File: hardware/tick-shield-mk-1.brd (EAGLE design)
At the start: 62 x 52 mm, 15 parts, among them IC1 DS1307, Y1 32.768kHz

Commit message: shieldify all the things
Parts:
- removed C3: 1uF, A_butts:C0805
- removed DISPLAY3, DISPLAY4: 7SEG_4DIGIT_COLON_APOS, A_butts:7SEG_4DIG_10MM
- removed Y1: 32.768kHz, A_butts:TC26H
- added R1, R2: 4.7k, A_butts:R0603
- C2: value 0.1uF -> 1uF; device A_butts:C0603 -> A_butts:C0805
- DISPLAY2: value 7SEG_4DIGIT_COLON_APOS -> 7SEG_4DIGIT_COLON14.2MM-CC; device A_butts:7SEG_4DIG_10MM -> A_butts:7SEG_4DIG_0.56IN_14MM_ADAFRUIT
- IC1: value DS1307 -> DS1338C; device A_butts:DIL08 -> A_butts:SO16W
- moved IC1 26.9 mm to (6.50, 35.5), flipped to the bottom, turned to 0 degrees
- moved C1 26.4 mm to (7.50, 28.0), flipped to the bottom
- moved BAT1 24.4 mm to (8.00, 16.5)
- moved C2 24.0 mm to (32.0, 47.0)
- moved H4 20.0 mm to (48.5, 49.5)
- moved SHIELD 20.0 mm to (6.00, 1.87)
- moved H3 20.0 mm to (48.5, 2.50)
- moved DISPLAY1 15.0 mm to (25.5, 35.5)
- moved H2 9.06 mm to (2.50, 49.5)
- moved H1 9.00 mm to (2.50, 2.50)
- moved DISPLAY2 8.51 mm to (25.5, 16.5)
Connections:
- removed net D10: DISPLAY1.P$13, DISPLAY2.14, DISPLAY3.1, SHIELD.D10
- removed net D11: DISPLAY1.P$9, DISPLAY2.16, DISPLAY3.2, SHIELD.D11
- removed net D12: DISPLAY1.P$4, DISPLAY2.13, DISPLAY3.6, SHIELD.D12
- removed net D13: DISPLAY1.P$2, DISPLAY2.3, DISPLAY3.8, SHIELD.D13
- removed net N$1: IC1.2, Y1.2
- removed net N$2: IC1.1, Y1.1
- net A0: now also DISPLAY1.P$13, DISPLAY2.P$1; no longer DISPLAY1.P$1, DISPLAY2.5, DISPLAY4.1
- net A1: now also DISPLAY1.P$9, DISPLAY2.P$12; no longer DISPLAY1.P$12, DISPLAY2.11, DISPLAY4.2
- net A2: now also DISPLAY1.P$4, DISPLAY2.P$5; no longer DISPLAY1.P$5, DISPLAY2.15, DISPLAY4.6
- net A3: now also DISPLAY1.P$2, DISPLAY2.P$3; no longer DISPLAY1.P$3, DISPLAY2.7, DISPLAY4.8
- net D2: now also DISPLAY1.P$1, DISPLAY2.P$14; no longer DISPLAY1.P$14, DISPLAY3.14, DISPLAY4.14
- net D3: now also DISPLAY1.P$12, DISPLAY2.P$11; no longer DISPLAY1.P$11, DISPLAY3.16, DISPLAY4.16
- net D4: now also DISPLAY1.P$5, DISPLAY2.P$10; no longer DISPLAY1.P$10, DISPLAY3.13, DISPLAY4.13
- net D5: now also DISPLAY1.P$3, DISPLAY2.P$6; no longer DISPLAY1.P$6, DISPLAY3.3, DISPLAY4.3
- net D6: now also DISPLAY1.P$14, DISPLAY2.P$13; no longer DISPLAY2.1, DISPLAY3.5, DISPLAY4.5
- net D7: now also DISPLAY1.P$11, DISPLAY2.P$9; no longer DISPLAY2.2, DISPLAY3.11, DISPLAY4.11
- net D8: now also DISPLAY1.P$10, DISPLAY2.P$4; no longer DISPLAY2.6, DISPLAY3.15, DISPLAY4.15
- net D9: now also DISPLAY1.P$6, DISPLAY2.P$2; no longer DISPLAY2.8, DISPLAY3.7, DISPLAY4.7
- net GND: now also IC1.10, IC1.11, IC1.12, IC1.13, IC1.15, IC1.5, IC1.6, IC1.7, IC1.8, IC1.9; no longer C3.2
- net N$3: now also IC1.14; no longer IC1.3
- net SCL: now also IC1.1, R2.1; no longer IC1.6
- net SDA: now also IC1.16, R1.1; no longer IC1.5
- net VCC: now also IC1.3, R1.2, R2.2; no longer C3.1, IC1.8
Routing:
- net D13: track 102.0 -> 0.00 mm, vias 1 -> 0
- net D12: track 92.8 -> 0.00 mm, vias 1 -> 0
- net D11: track 76.5 -> 0.00 mm
- net D7: track 82.3 -> 11.0 mm, vias 3 -> 0
- net D10: track 67.5 -> 0.00 mm, vias 1 -> 0
- net A2: track 102.4 -> 36.1 mm, vias 2 -> 1
- net D8: track 62.7 -> 4.81 mm, vias 3 -> 0
- net D6: track 75.0 -> 28.5 mm, vias 1 -> 0
- net A3: track 78.0 -> 32.3 mm, vias 2 -> 0
- net VCC: track 83.1 -> 43.4 mm, vias 1 -> 0
- net D5: track 74.4 -> 38.0 mm
- net A0: track 63.5 -> 30.8 mm, vias 2 -> 1
- net SDA: track 46.9 -> 15.5 mm, vias 1 -> 0
- net A1: track 63.2 -> 32.2 mm
- net D3: track 45.0 -> 14.8 mm, vias 1 -> 0
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- removed copper zone on layer 1, net GND
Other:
- board size 62 x 52 mm -> 51 x 52 mm

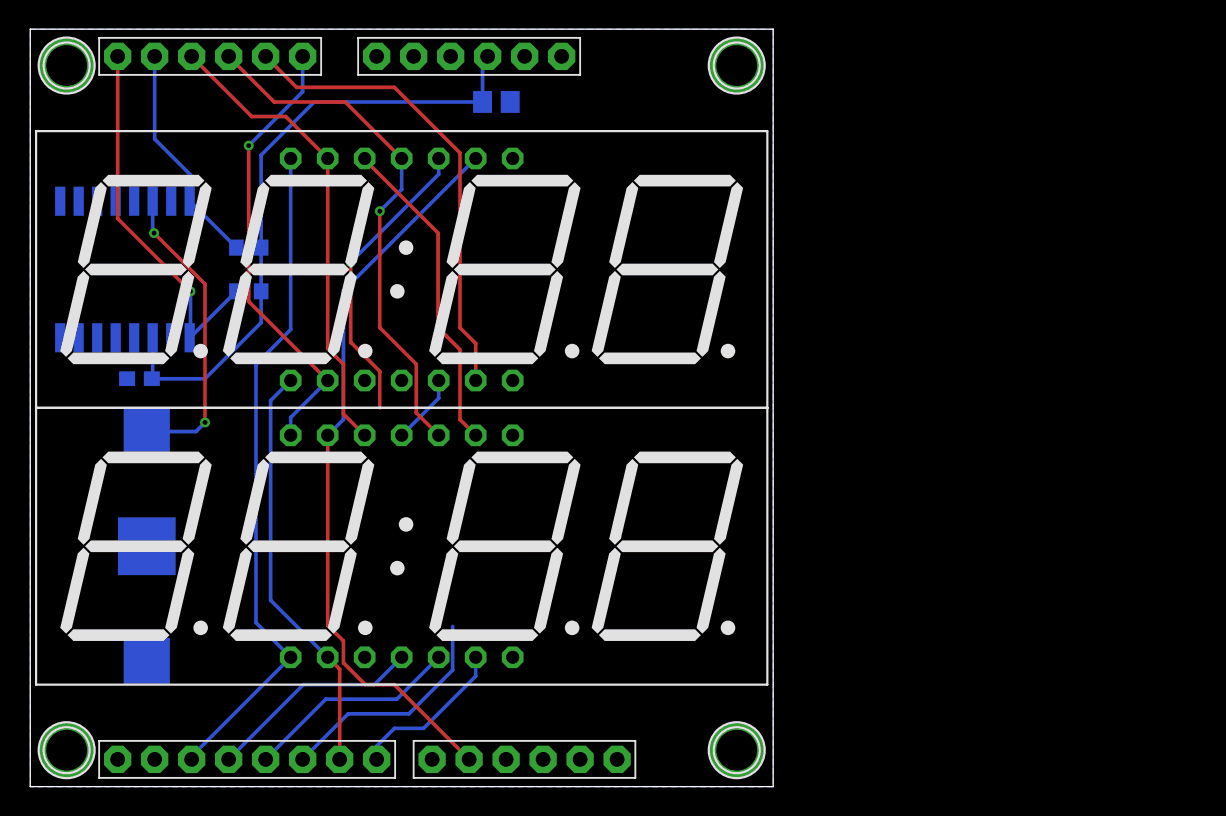
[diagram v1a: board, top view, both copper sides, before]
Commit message: going for a fully integrated board now using charlieplexing
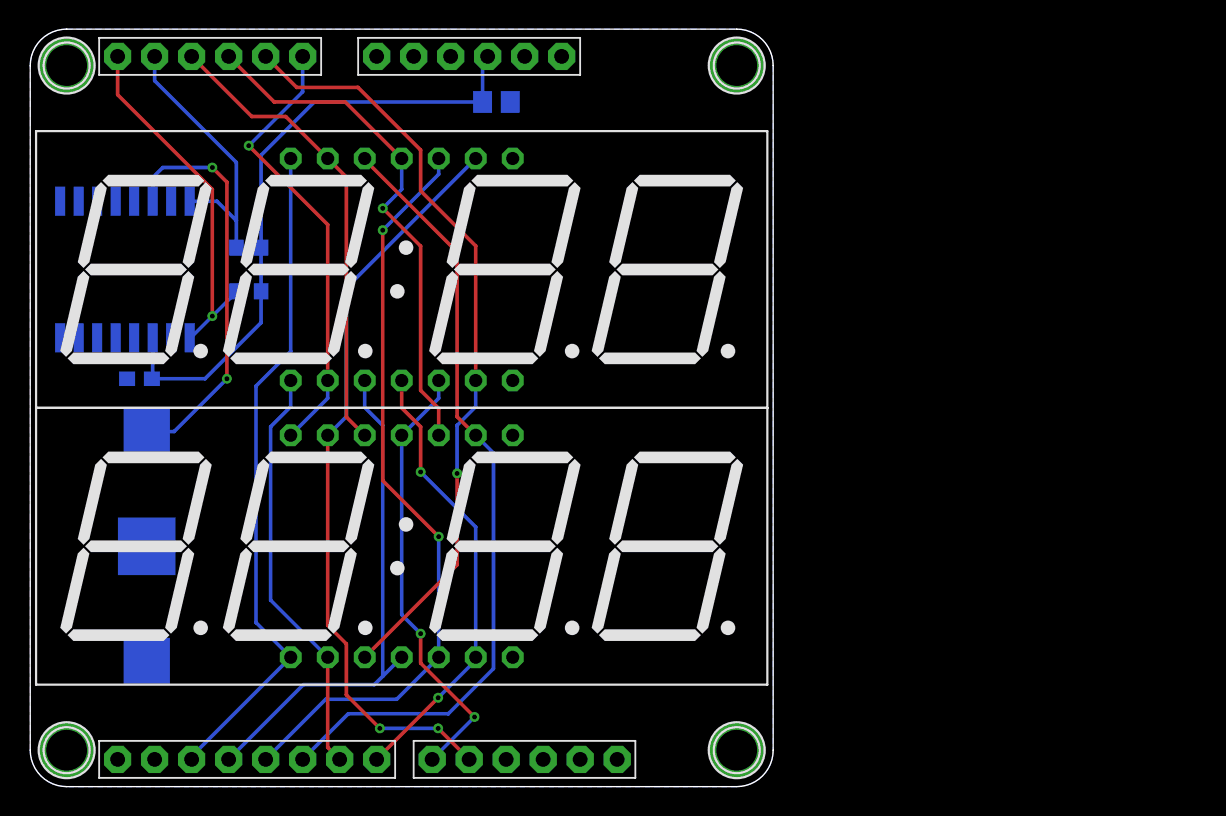
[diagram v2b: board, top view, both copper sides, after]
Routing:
- net D8: track 4.81 -> 30.3 mm, vias 0 -> 2
- net D3: track 14.8 -> 35.6 mm
- net A1: track 32.2 -> 52.8 mm, vias 0 -> 1
- net D7: track 11.0 -> 30.9 mm, vias 0 -> 2
- net D4: track 35.2 -> 52.2 mm, vias 1 -> 2
- net D5: track 38.0 -> 54.4 mm
- net N$3: track 20.9 -> 27.9 mm
- net SDA: track 15.5 -> 19.2 mm
- net D9: track 50.7 -> 51.8 mm, vias 0 -> 2
- net SCL: track 25.9 -> 25.1 mm
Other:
- outline, holes or cut-outs redrawn
